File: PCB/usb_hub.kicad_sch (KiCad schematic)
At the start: 29 parts, among them J1 918-418K2023S40001, J2 901-211A1021D10100, J3 901-211A1021D10100, U4 GL852G-OHY60, Y1 12MHz

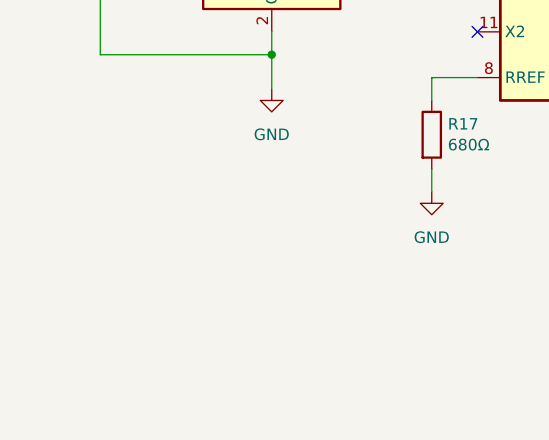
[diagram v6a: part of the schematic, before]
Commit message: Improve the ESD protection
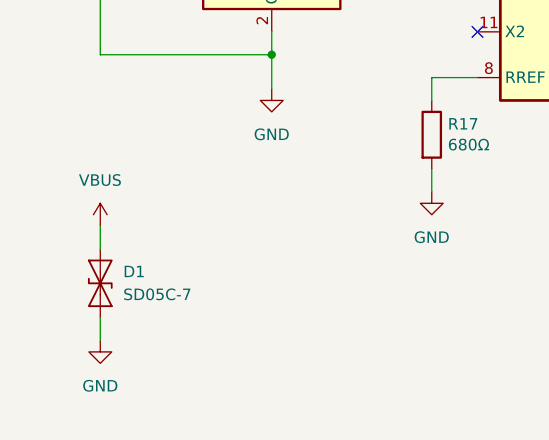
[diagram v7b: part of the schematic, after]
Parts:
- added D1: SD05C-7, Diode_SMD:D_SOD-323, symbol Diode:SD05_SOD323
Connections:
- net GND: now also D1.1 (A1)
- net VBUS: now also D1.2 (A2)
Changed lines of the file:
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@@
 	(wire
 		(pts
+			(xy 44.45 158.75) (xy 44.45 161.29)
+		)
+		(stroke
+			(width 0)
+			(type default)
+		)
+	)
+	(wire
+		(pts
 			(xy 260.35 153.67) (xy 260.35 156.21)
 		)
@@
 	(wire
 		(pts
+			(xy 44.45 171.45) (xy 44.45 168.91)
+		)
+		(stroke
+			(width 0)
+			(type default)
+		)
+	)
+	(wire
+		(pts
 			(xy 119.38 144.78) (xy 129.54 144.78)
 		)
@@
 	(symbol
 		(lib_id "power:GND")
+		(at 44.45 171.45 0)
+		(unit 1)
+		(exclude_from_sim no)
+		(in_bom yes)
+		(on_board yes)
+		(dnp no)
+		(fields_autoplaced yes)
+		(property "Reference" "#PWR029"
+			(at 44.45 177.8 0)
+			(effects
+				(font
+					(size 1.27 1.27)
+				)
+				(hide yes)
+			)
+		)
+		(property "Value" "GND"
+			(at 44.45 176.53 0)
+			(effects
+				(font
+					(size 1.27 1.27)
+				)
+			)
+		)
+		(property "Footprint" ""
+			(at 44.45 171.45 0)
+			(effects
+				(font
+					(size 1.27 1.27)
+				)
+				(hide yes)
+			)
+		)
+		(property "Datasheet" ""
+			(at 44.45 171.45 0)
+			(effects
+				(font
+					(size 1.27 1.27)
+				)
+				(hide yes)
+			)
+		)
+		(property "Description" "Power symbol creates a global label with name \"GND\" , ground"
+			(at 44.45 171.45 0)
+			(effects
+				(font
+					(size 1.27 1.27)
+				)
+				(hide yes)
+			)
+		)
+		(pin "1"
+		)
+		(instances
+			(project "clavier"
+				(path "/6362c6e0-59ef-40d3-b6e0-7e9dfe7b9b20/f3d926d4-179d-4033-9062-145e3f3d7f6d"
+					(reference "#PWR029")
+					(unit 1)
+				)
+			)
+		)
+	)
+	(symbol
+		(lib_id "power:GND")
 		(at 146.05 83.82 0)
 		(unit 1)
@@
 	)
 	(symbol
+		(lib_id "Diode:SD05_SOD323")
+		(at 44.45 165.1 90)
+		(unit 1)
+		(exclude_from_sim no)
+		(in_bom yes)
+		(on_board yes)
+		(dnp no)
+		(fields_autoplaced yes)
+		(property "Reference" "D1"
+			(at 46.99 163.8299 90)
+			(effects
+				(font
+					(size 1.27 1.27)
+				)
+				(justify right)
+			)
+		)
+		(property "Value" "SD05C-7"
+			(at 46.99 166.3699 90)
+			(effects
+				(font
+					(size 1.27 1.27)
+				)
+				(justify right)
+			)
+		)
+		(property "Footprint" "Diode_SMD:D_SOD-323"
+			(at 49.53 165.1 0)
+			(effects
+				(font
+					(size 1.27 1.27)
+				)
+				(hide yes)
+			)
+		)
+		(property "Datasheet" "https://www.lcsc.com/datasheet/lcsc_datasheet_2201272230_Diodes-Incorporated-SD05C-7_C1869324.pdf"
+			(at 44.45 165.1 0)
+			(effects
+				(font
+					(size 1.27 1.27)
+				)
+				(hide yes)
+			)
+		)
+		(property "Description" "5V, 450W Discrete Bidirectional TVS Diode, SOD-323"
+			(at 44.45 165.1 0)
+			(effects
+				(font
+					(size 1.27 1.27)
+				)
+				(hide yes)
+			)
+		)
+		(property "LCSC" "C1869324"
+			(at 44.45 165.1 90)
+			(effects
+				(font
+					(size 1.27 1.27)
+				)
+				(hide yes)
+			)
+		)
+		(property "Part_number" "SD05C-7"
+			(at 44.45 165.1 90)
+			(effects
+				(font
+					(size 1.27 1.27)
+				)
+				(hide yes)
+			)
+		)
+		(pin "1"
+		)
+		(pin "2"
+		)
+		(instances
+			(project ""
+				(path "/6362c6e0-59ef-40d3-b6e0-7e9dfe7b9b20/f3d926d4-179d-4033-9062-145e3f3d7f6d"
+					(reference "D1")
+					(unit 1)
+				)
+			)
+		)
+	)
+	(symbol
 		(lib_id "Device:C")
 		(at 146.05 49.53 0)
@@
 					(unit 1)
 				)
+			)
+		)
+	)
+	(symbol
+		(lib_id "power:VBUS")
+		(at 44.45 158.75 0)
+		(unit 1)
+		(exclude_from_sim no)
+		(in_bom yes)
+		(on_board yes)
+		(dnp no)
+		(fields_autoplaced yes)
+		(property "Reference" "#PWR028"
+			(at 44.45 162.56 0)
+			(effects
+				(font
+					(size 1.27 1.27)
+				)
+				(hide yes)
+			)
+		)
+		(property "Value" "VBUS"
+			(at 44.45 153.67 0)
+			(effects
+				(font
+					(size 1.27 1.27)
+				)
+			)
+		)
+		(property "Footprint" ""
+			(at 44.45 158.75 0)
+			(effects
+				(font
+					(size 1.27 1.27)
+				)
+				(hide yes)
+			)
+		)
+		(property "Datasheet" ""
+			(at 44.45 158.75 0)
+			(effects
+				(font
+					(size 1.27 1.27)
+				)
+				(hide yes)
+			)
+		)
+		(property "Description" "Power symbol creates a global label with name \"VBUS\""
+			(at 44.45 158.75 0)
+			(effects
+				(font
+					(size 1.27 1.27)
+				)
+				(hide yes)
+			)
+		)
+		(pin "1"
+		)
+		(instances
+			(project "clavier"
+				(path "/6362c6e0-59ef-40d3-b6e0-7e9dfe7b9b20/f3d926d4-179d-4033-9062-145e3f3d7f6d"
+					(reference "#PWR028")
+					(unit 1)
+				)

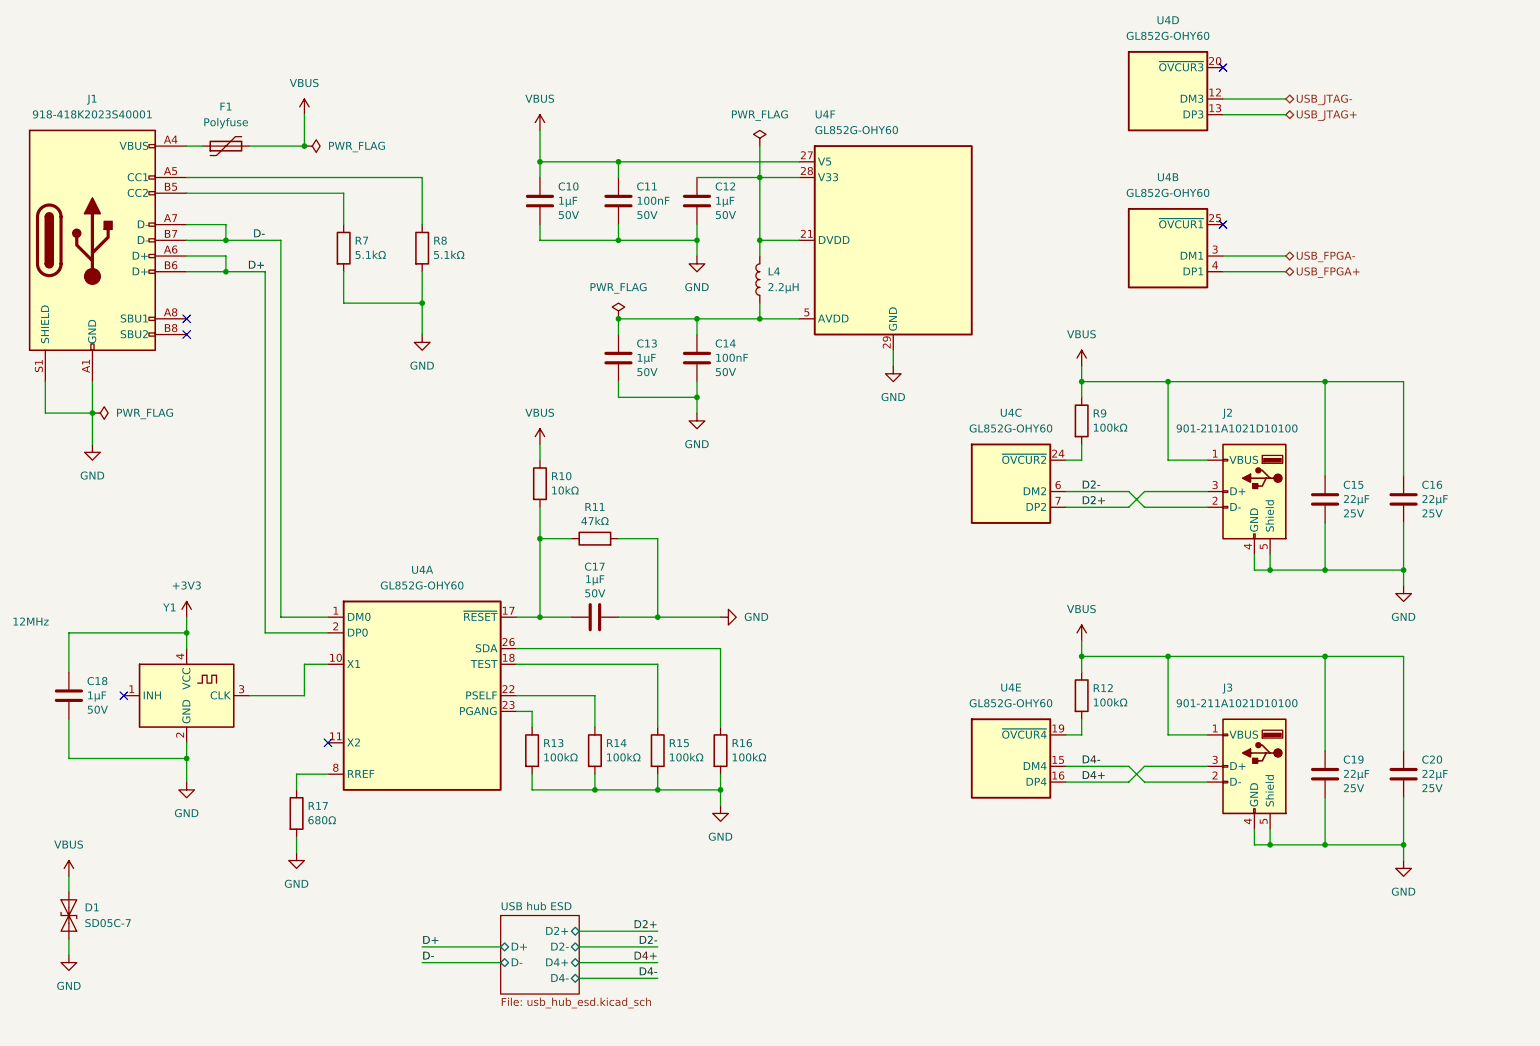
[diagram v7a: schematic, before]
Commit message: Complete the PCB routing
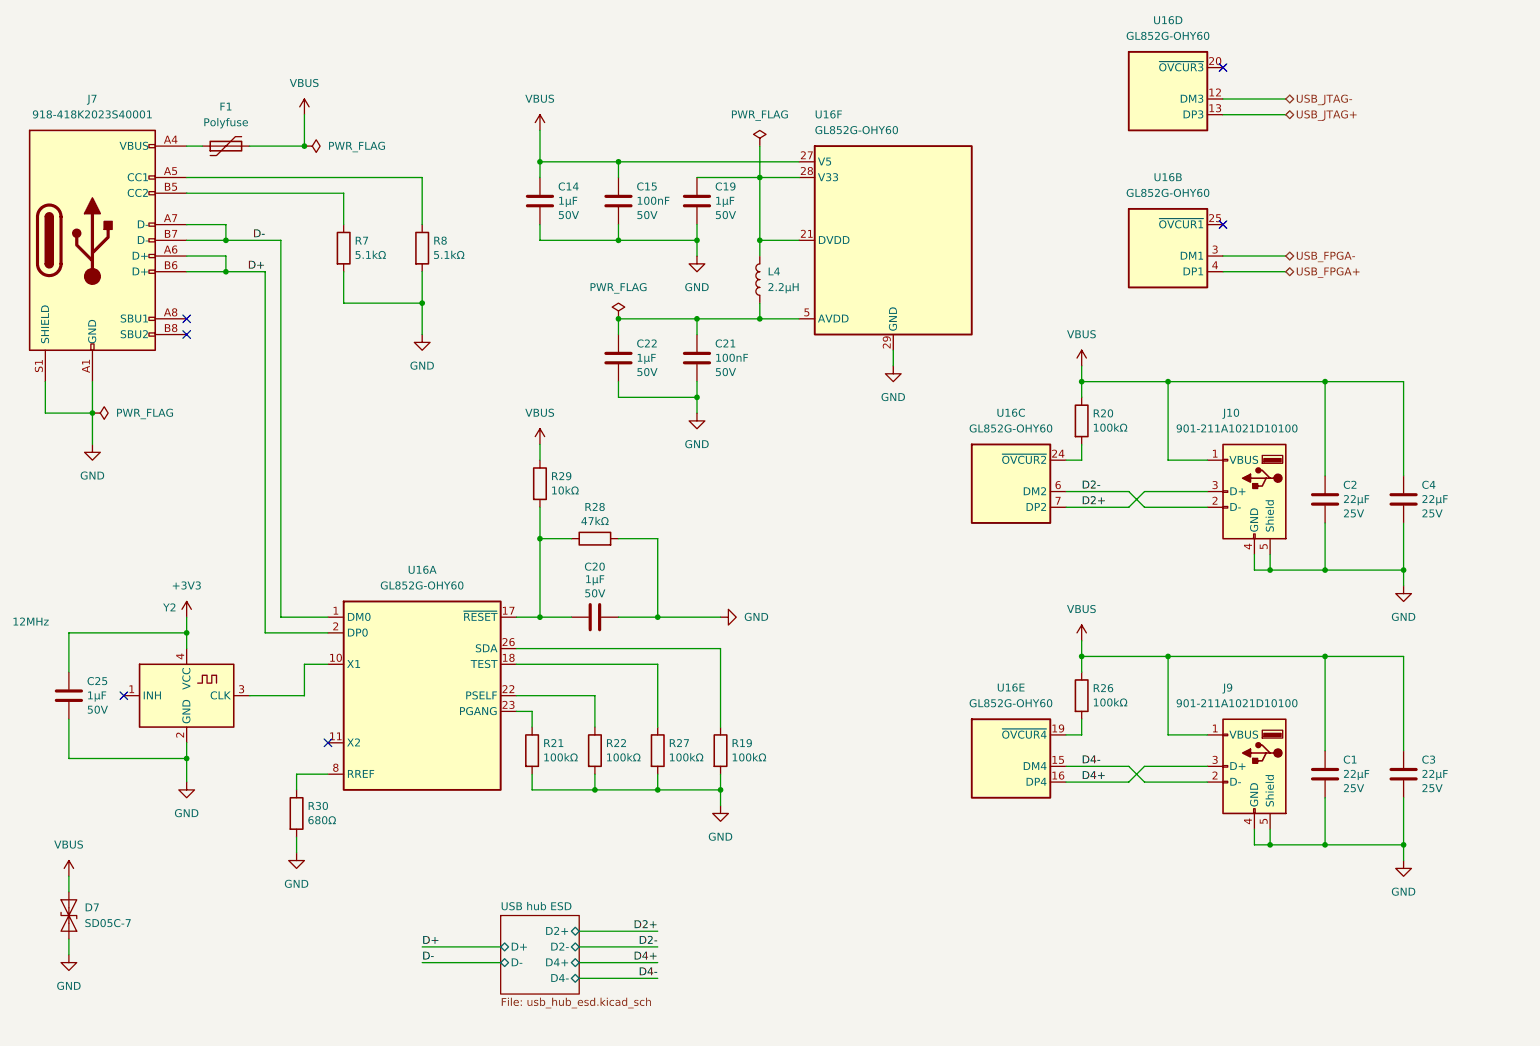
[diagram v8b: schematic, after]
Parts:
- renumbered C19 to C1, C10 to C14, C11 to C15, C12 to C19, C15 to C2, C17 to C20, C14 to C21, C13 to C22, C18 to C25, C20 to C3, C16 to C4, D1 to D7, J2 to J10, J1 to J7, J3 to J9, R16 to R19, R9 to R20, R13 to R21, R14 to R22, R12 to R26, R15 to R27, R11 to R28, R10 to R29, R17 to R30, U4 to U16, Y1 to Y2
